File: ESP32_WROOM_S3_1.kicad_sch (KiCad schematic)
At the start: 19 parts, among them J1 USB_C_Receptacle_USB2.0_16P, SW1 SW_Push, SW2 SW_Push, U1 ESP32-S3-WROOM-1, U2 LD1117S33TR_SOT223

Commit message: Add files via upload
Updated BQ76952 schematic with passive cell balancing, voltage readout to ESP32 and temperature sensing. To do: Connect remaining pins on BQ76952 to ESP32.
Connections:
- net IO41 renamed BAT_ADC
- net IO48 renamed BATS_EN
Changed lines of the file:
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@@
 	(rectangle
 		(start 115.57 63.5)
-		(end 173.99 144.78)
+		(end 180.34 144.78)
 		(stroke
 			(width 0)
@@
 	(wire
 		(pts
+			(xy 158.75 116.84) (xy 167.64 116.84)
+		)
+		(stroke
+			(width 0)
+			(type default)
+		)
+	)
+	(wire
+		(pts
 			(xy 59.69 142.24) (xy 72.39 142.24)
 		)
@@
 		(pts
 			(xy 85.09 147.32) (xy 85.09 149.86)
+		)
+		(stroke
+			(width 0)
+			(type default)
+		)
+	)
+	(wire
+		(pts
+			(xy 158.75 129.54) (xy 167.64 129.54)
 		)
 		(stroke
@@
 		)
 	)
+	(global_label "BATS_EN"
+		(shape output)
+		(at 167.64 129.54 0)
+		(fields_autoplaced yes)
+		(effects
+			(font
+				(size 1.27 1.27)
+			)
+			(justify left)
+		)
+		(property "Intersheetrefs" "${INTERSHEET_REFS}"
+			(at 178.608 129.54 0)
+			(hide yes)
+			(show_name no)
+			(do_not_autoplace no)
+			(effects
+				(font
+					(size 1.27 1.27)
+				)
+				(justify left)
+			)
+		)
+	)
+	(global_label "BAT_ADC"
+		(shape input)
+		(at 167.64 116.84 0)
+		(fields_autoplaced yes)
+		(effects
+			(font
+				(size 1.27 1.27)
+			)
+			(justify left)
+		)
+		(property "Intersheetrefs" "${INTERSHEET_REFS}"
+			(at 178.5476 116.84 0)
+			(hide yes)
+			(show_name no)
+			(do_not_autoplace no)
+			(effects
+				(font
+					(size 1.27 1.27)
+				)
+				(justify left)
+			)
+		)
+	)

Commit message: REV1 PCB that was sent to production (PCBWAY)
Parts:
- removed C2, C5: 100n, symbol Device:C
- removed C3: 22u, symbol Device:C
- removed C4: 10u, symbol Device:C
- removed D3: BLUE, symbol Device:LED
- removed R4: 5.1k, symbol Device:R_US
- removed U2: LD1117S33TR_SOT223, Package_TO_SOT_SMD:SOT-223-3_TabPin2, symbol Regulator_Linear:LD1117S33TR_SOT223
- added C2, C3: 100uF, Capacitor_SMD:CP_Elec_6.3x5.8, symbol Device:C_Polarized_Small_US
- added C35, C38: 10u, Capacitor_SMD:C_0805_2012Metric, symbol Device:C
- added C36, C39: 22u, Capacitor_SMD:C_0805_2012Metric, symbol Device:C
- added C4: 220uF, Capacitor_SMD:CP_Elec_6.3x5.8, symbol Device:C_Polarized_Small_US
- added J2, J3, J5: Conn_01x07_Socket, Connector_JST:JST_XH_B7B-XH-A_1x07_P2.50mm_Vertical, symbol Connector:Conn_01x07_Socket
- added J4: Conn_01x02_Socket, Connector_JST:JST_XH_B2B-XH-A_1x02_P2.50mm_Vertical, symbol Connector:Conn_01x02_Socket
- added L2: 2.2uH, Inductor_SMD:L_Wuerth_MAPI-3020, symbol Device:L_Small
- added L3: 1.5uH, Inductor_SMD:L_Wuerth_MAPI-3020, symbol Device:L_Small
- added R69, R73: 100k, Resistor_SMD:R_0805_2012Metric, symbol Device:R_Small_US
- added R70: 240k, Resistor_SMD:R_0805_2012Metric, symbol Device:R_Small_US
- added R71: 750k, Resistor_SMD:R_0805_2012Metric, symbol Device:R_Small_US
- added R72: 453k, Resistor_SMD:R_0805_2012Metric, symbol Device:R_Small_US
- added SW3: SPDT_Slide_PTH_11.6x4.0mm, PCM_SparkFun-Switch:Slide_SPDT_PTH_11.6x4.0mm, symbol PCM_SparkFun-Switch:SPDT_Slide_PTH_11.6x4.0mm
- added TP45, TP46, TP47, TP48, TP49, TP50, TP51, TP52, TP53, TP54, TP55, TP56, TP57: TestPoint, TestPoint:TestPoint_Pad_D1.0mm, symbol Connector:TestPoint
- added U2: TPS62170DSG, Package_SON:WSON-8-1EP_2x2mm_P0.5mm_EP0.9x1.6mm_ThermalVias, symbol Regulator_Switching:TPS62170DSG
- added U4: TLV62569DBV, Package_TO_SOT_SMD:SOT-23-5, symbol Regulator_Switching:TLV62569DBV
- C1: footprint (none) -> Capacitor_SMD:C_0805_2012Metric
- D1, D2: footprint (none) -> LED_SMD:LED_0805_2012Metric
- J1: footprint (none) -> Connector_USB:USB_C_Receptacle_GCT_USB4105-xx-A_16P_TopMnt_Horizontal
- R1, R2, R3: footprint (none) -> Resistor_SMD:R_0805_2012Metric
- R5, R6: value 5.1k -> 200; footprint (none) -> Resistor_SMD:R_0805_2012Metric
- SW1, SW2: footprint (none) -> PCM_SparkFun-Switch:Push_SMD_4.2x3.2mm
- U1: now left out of the parts list
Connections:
- net +3V3: now also C4.1, SW3.2 (B)
- net BATS_EN: now also TP53.1
- net BAT_ADC: now also TP54.1
- net IO10: now also J2.4 (Pin_4)
- net IO13: now also J2.5 (Pin_5)
- net IO14: now also J2.6 (Pin_6)
- net IO15: now also J2.7 (Pin_7)
- net IO16: now also J3.1 (Pin_1)
- net IO17: now also J3.2 (Pin_2)
- net IO18: now also J3.3 (Pin_3)
- net IO21: now also J3.4 (Pin_4)
- net IO3: now also J2.1 (Pin_1)
- net IO35: now also J3.5 (Pin_5)
- net IO36: now also J3.6 (Pin_6)
- net IO37: now also J3.7 (Pin_7)
- net IO38: now also J5.1 (Pin_1)
- net IO39: now also J5.2 (Pin_2)
- net IO40: now also J5.3 (Pin_3)
- net IO42: now also J5.7 (Pin_7)
- net IO45: now also J5.6 (Pin_6)
- net IO46: now also J5.5 (Pin_5)
- net IO47: now also J5.4 (Pin_4)
- net IO7: now also J2.2 (Pin_2)
- net IO8: now also J2.3 (Pin_3)
- net RXD0: now also J4.2 (Pin_2)
- net TXD0: now also J4.1 (Pin_1)
- net at D1.2 (A): now also R5.2
- net at R6.2: now also D2.2 (A)
- net +5V renamed VUSB
- net VUSB: now also C38.1, U4.1 (EN), U4.4 (VIN)
- net GND renamed VSS
- net VSS: now also C2.2, C3.2, C35.2, C36.2, C38.2, C39.2, C4.2, R70.2, R73.2, U2.1 (PGND), U2.4 (AGND), U2.9 (PAD), U4.2 (GND)
- net IO1 renamed DCHG
- net DCHG: now also TP45.1
- net IO11 renamed SDA
- net SDA: now also TP51.1
- net IO12 renamed SCL
- net SCL: now also TP52.1
- net IO2 renamed DDSG
- net DDSG: now also TP46.1
- net IO4 renamed ALERT
- net ALERT: now also TP47.1
- net IO5 renamed SHUT
- net SHUT: now also TP48.1
- net IO6 renamed FUSE
- net FUSE: now also TP49.1
- net IO9 renamed DFETOFF
- net DFETOFF: now also TP50.1
- new net: R72.2, R73.1, U4.5 (FB)
- new net: L2.1, U2.7 (SW)
- new net: L3.1, U4.3 (SW)
- new net: R70.1, R71.2, TP57.1, U2.5 (FB)
- new net: R69.2, U2.8 (PG)
- new net +BATT: C35.1, TP56.1, U2.2 (VIN), U2.3 (EN)
- new net BATT_3V3_PWR: C3.1, C36.1, L2.2, R69.1, R71.1, SW3.1 (A), TP55.1, U2.6 (VOS)
- new net USB_3V3_PWR: C2.1, C39.1, L3.2, R72.1, SW3.3 (C)
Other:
- moved on the sheet: C1, D1, D2, R1, R5, R6, SW1, SW2, U1

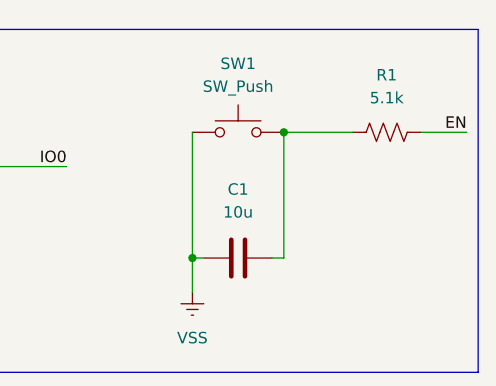
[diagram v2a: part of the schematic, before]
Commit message: These files are for the final report
NOTE:
1. PCB has mixed up nets so many traces going to the BQ76952 are DISCONNECTED.
2. BOTH active and passive balancing are connected in parallel even though only active balancing is supposed to be connected.
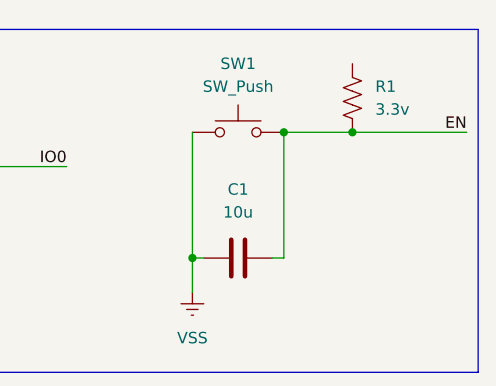
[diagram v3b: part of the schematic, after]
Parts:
- R1: value 5.1k -> 3.3v
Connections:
- net EN: now also C1.2, R1.1, SW1.2; no longer R1.2
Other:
- moved on the sheet: R1
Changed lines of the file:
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@@
 	)
 	(junction
+		(at 254 29.21)
+		(diameter 0)
+		(color 0 0 0 0)
+	)
+	(junction
 		(at 74.93 102.87)
 		(diameter 0)
@@
 	(wire
 		(pts
+			(xy 254 29.21) (xy 266.7 29.21)
+		)
+		(stroke
+			(width 0)
+			(type default)
+		)
+	)
+	(wire
+		(pts
 			(xy 38.1 90.17) (xy 43.18 90.17)
 		)
@@
 	(wire
 		(pts
-			(xy 266.7 29.21) (xy 261.62 29.21)
-		)
-		(stroke
-			(width 0)
-			(type default)
-		)
-	)
-	(wire
-		(pts
 			(xy 132.08 43.18) (xy 132.08 48.26)
 		)
@@
 	(symbol
 		(lib_id "Device:R_US")
-		(at 257.81 29.21 90)
+		(at 254 25.4 180)
 		(unit 1)
 		(body_style 1)
@@
 		(fields_autoplaced yes)
 		(property "Reference" "R1"
-			(at 257.81 22.86 90)
+			(at 256.54 24.1299 0)
 			(show_name no)
 			(do_not_autoplace no)
@@
 					(size 1.27 1.27)
 				)
+				(justify right)
 			)
 		)
-		(property "Value" "5.1k"
-			(at 257.81 25.4 90)
+		(property "Value" "3.3v"
+			(at 256.54 26.6699 0)
 			(show_name no)
 			(do_not_autoplace no)
@@
 					(size 1.27 1.27)
 				)
+				(justify right)
 			)
 		)
 		(property "Footprint" "Resistor_SMD:R_0805_2012Metric"
-			(at 258.064 28.194 90)
+			(at 252.984 25.146 90)
 			(hide yes)
 			(show_name no)
@@
 		)
 		(property "Datasheet" ""
-			(at 257.81 29.21 0)
+			(at 254 25.4 0)
 			(hide yes)
 			(show_name no)
@@
 		)
 		(property "Description" "Resistor, US symbol"
-			(at 257.81 29.21 0)
+			(at 254 25.4 0)
 			(hide yes)
 			(show_name no)
